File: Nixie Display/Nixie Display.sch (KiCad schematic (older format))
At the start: 34 parts, among them J1 Conn_01x06_Male, J10 Conn_01x02_Male, J12 Conn_01x02_Male, J2 Conn_01x02_Male, J3 Conn_01x20_Male, J4 Conn_01x02_Male, J5 Conn_01x20_Male, J6 Conn_01x02_Male, J7 Conn_01x20_Male, J8 Conn_01x02_Male, U1 WS2812B, U2 WS2812B, U3 WS2812B, U4 WS2812B, U5 WS2812B, U6 WS2812B

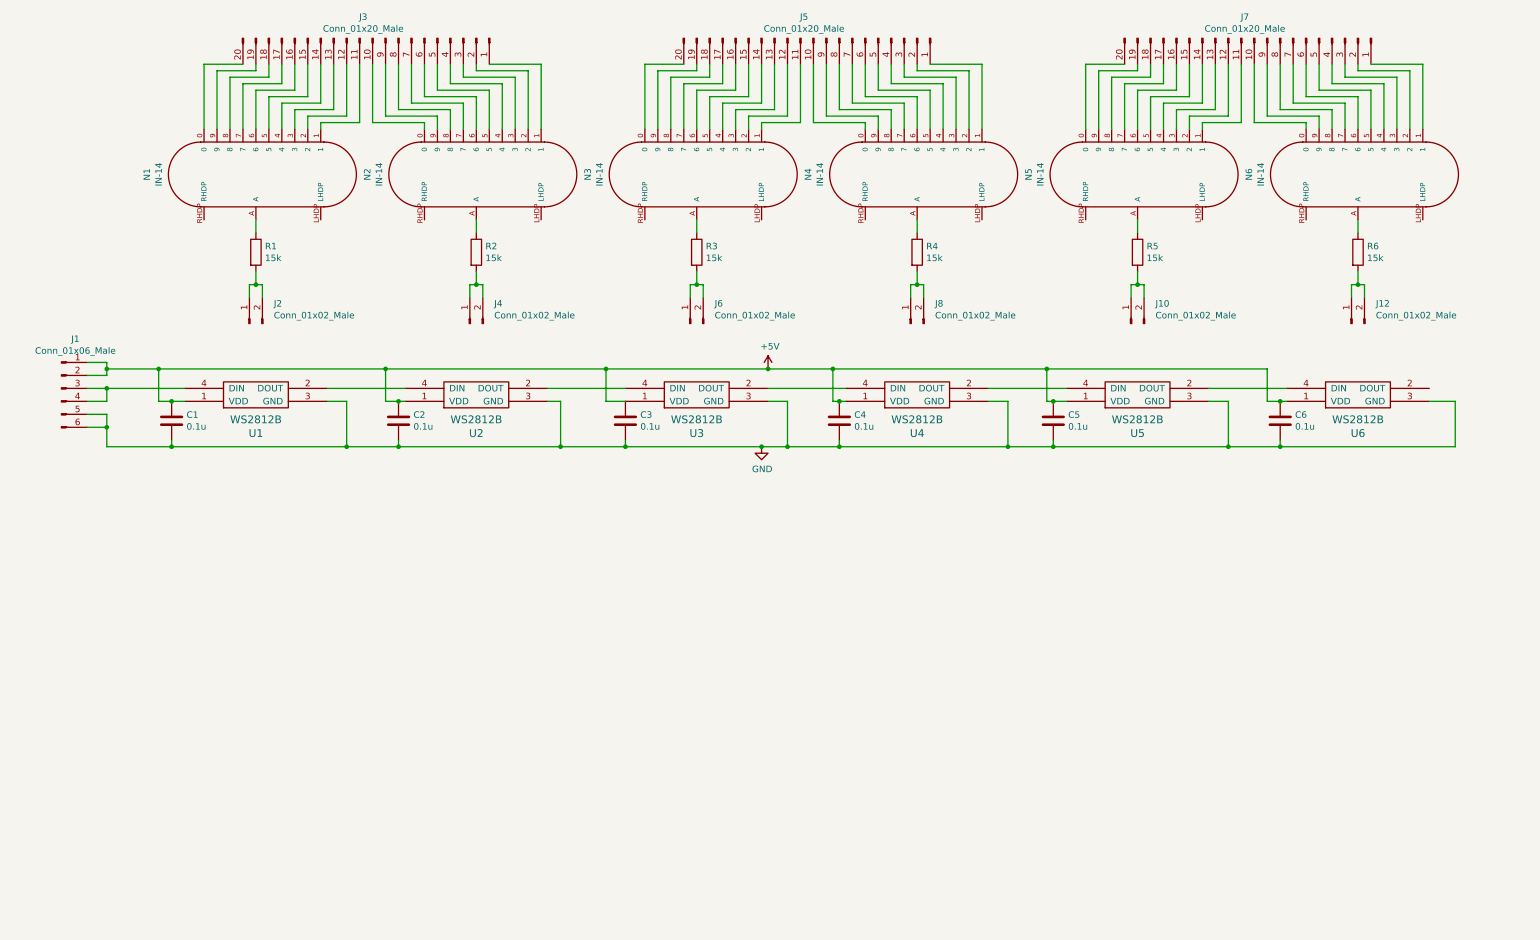
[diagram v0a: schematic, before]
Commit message: Final V1.0 design. Different sized boards for top and bottom layer. Goal for v2.0 is to have matching top and bottom pcbas
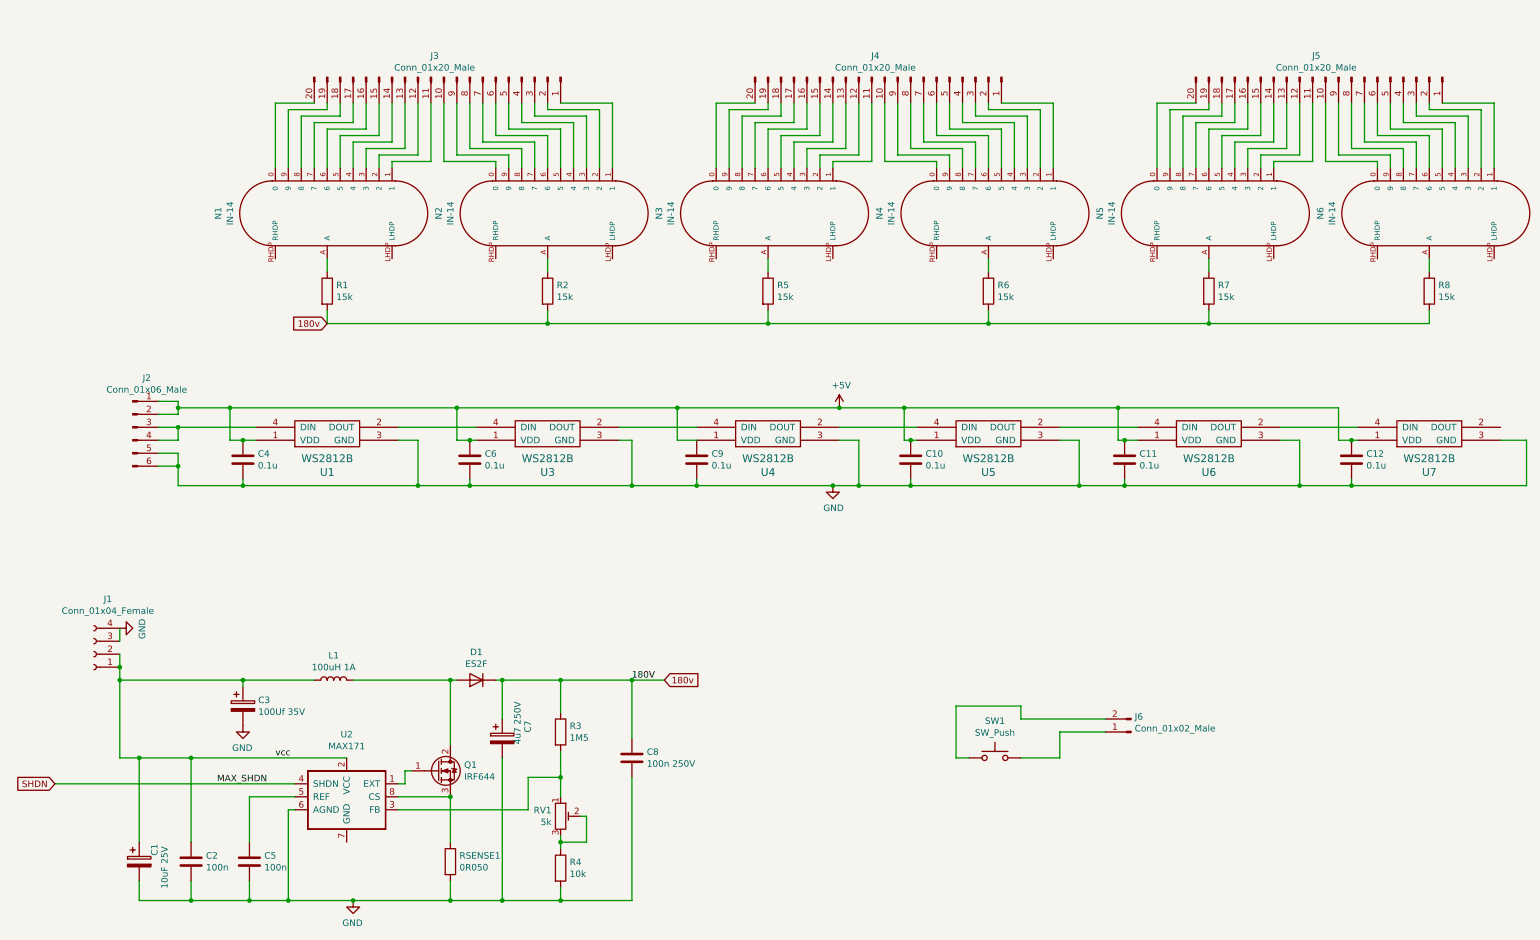
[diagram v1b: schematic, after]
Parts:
- removed C1, C3: 0.1u, Capacitor_SMD:C_0603_1608Metric_Pad1.05x0.95mm_HandSolder, symbol Device:C
- removed J1: Conn_01x06_Male, Connector_PinHeader_2.54mm:PinHeader_1x06_P2.54mm_Vertical, symbol Connector:Conn_01x06_Male
- removed J10, J12, J2, J4, J8: Conn_01x02_Male, Connector_PinHeader_2.54mm:PinHeader_1x02_P2.54mm_Vertical_SMD_Pin1Left, symbol Connector:Conn_01x02_Male
- removed J7: Conn_01x20_Male, Connector_PinHeader_2.54mm:PinHeader_1x20_P2.54mm_Vertical_SMD_Pin1Left, symbol Connector:Conn_01x20_Male
- removed U2: WS2812B, LED_SMD:LED_WS2812B_PLCC4_5.0x5.0mm_P3.2mm, symbol ws2812:WS2812B
- added C1: 10uF 25V, Capacitor_Tantalum_SMD:CP_EIA-7343-31_Kemet-D_Pad2.25x2.55mm_HandSolder, symbol Device:CP
- added C10, C11, C12, C9: 0.1u, Capacitor_SMD:C_0603_1608Metric_Pad1.05x0.95mm_HandSolder, symbol Device:C
- added C3: 100Uf 35V, Capacitor_Tantalum_SMD:CP_EIA-7343-31_Kemet-D_Pad2.25x2.55mm_HandSolder, symbol Device:CP
- added C7: 4u7 250V, Capacitor_SMD:CP_Elec_10x14.3, symbol Device:CP
- added C8: 100n 250V, Capacitor_SMD:C_2220_5650Metric_Pad1.97x5.40mm_HandSolder, symbol Device:C
- added D1: ES2F, Nixie Power and Logic:D_SOD-214AA, symbol Device:D
- added J1: Conn_01x04_Female, Connector_PinHeader_2.54mm:PinHeader_1x04_P2.54mm_Vertical_SMD_Pin1Left, symbol Connector:Conn_01x04_Female
- added J2: Conn_01x06_Male, Connector_PinHeader_2.54mm:PinHeader_1x06_P2.54mm_Vertical, symbol Connector:Conn_01x06_Male
- added J4: Conn_01x20_Male, Connector_PinHeader_2.54mm:PinHeader_1x20_P2.54mm_Vertical_SMD_Pin1Left, symbol Connector:Conn_01x20_Male
- added L1: 100uH 1A, Inductor_SMD:L_Bourns_SDR1806, symbol Device:L
- added Q1: IRF644, Package_TO_SOT_THT:TO-220-3_Vertical, symbol Transistor_FET:BUZ11
- added R7, R8: 15k, Resistor_SMD:R_0603_1608Metric_Pad1.05x0.95mm_HandSolder, symbol Device:R
- added RSENSE1: 0R050, Resistor_SMD:R_2010_5025Metric_Pad1.52x2.65mm_HandSolder, symbol Device:R
- added RV1: 5k, Potentiometer_SMD:Potentiometer_Bourns_3214W_Vertical, symbol Nixie-Display-rescue:R_POT_TRIM-Device_Eric
- added SW1: SW_Push, Button_Switch_SMD:SW_SPST_B3S-1000, symbol Switch:SW_Push
- added U2: MAX171, Nixie Power and Logic:SOIC−8-NARROW, symbol Nixie-Display-rescue:MAX171-Device_Eric
- added U7: WS2812B, LED_SMD:LED_WS2812B_PLCC4_5.0x5.0mm_P3.2mm, symbol ws2812:WS2812B
- C2, C5: value 0.1u -> 100n; footprint Capacitor_SMD:C_0603_1608Metric_Pad1.05x0.95mm_HandSolder -> Capacitor_SMD:C_0805_2012Metric_Pad1.15x1.40mm_HandSolder
- R3: value 15k -> 1M5; footprint Resistor_SMD:R_0603_1608Metric_Pad1.05x0.95mm_HandSolder -> Resistor_SMD:R_2512_6332Metric_Pad1.52x3.35mm_HandSolder
- R4: value 15k -> 10k; footprint Resistor_SMD:R_0603_1608Metric_Pad1.05x0.95mm_HandSolder -> Resistor_SMD:R_0805_2012Metric_Pad1.15x1.40mm_HandSolder
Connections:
- net +5V: now also C10.1, C11.1, C12.1, C9.1, J2.1 (Pin_1), J2.2 (Pin_2), U7.1 (VDD); no longer C2.1, C5.1
- net GND: now also R4.2, C1.2, C10.2, C11.2, C12.2, C3.2, C7.2, C8.2, C9.2, J1.3 (Pin_3), J1.4 (Pin_4), J2.5 (Pin_5), J2.6 (Pin_6), RSENSE1.2, U2.6 (AGND), U7.3 (GND)
- net at N3.0: now also J4.20 (Pin_20); no longer J5.20 (Pin_20)
- net at N3.1: now also J4.11 (Pin_11); no longer J5.11 (Pin_11)
- net at N3.2: now also J4.12 (Pin_12); no longer J5.12 (Pin_12)
- net at N3.3: now also J4.13 (Pin_13); no longer J5.13 (Pin_13)
- net at N3.4: now also J4.14 (Pin_14); no longer J5.14 (Pin_14)
- net at N3.5: now also J4.15 (Pin_15); no longer J5.15 (Pin_15)
- net at N3.6: now also J4.16 (Pin_16); no longer J5.16 (Pin_16)
- net at N3.7: now also J4.17 (Pin_17); no longer J5.17 (Pin_17)
- net at N3.8: now also J4.18 (Pin_18); no longer J5.18 (Pin_18)
- net at N3.9: now also J4.19 (Pin_19); no longer J5.19 (Pin_19)
- net at N3.A: now also R5.1; no longer R3.1
- net at N4.0: now also J4.10 (Pin_10); no longer J5.10 (Pin_10)
- net at N4.1: now also J4.1 (Pin_1); no longer J5.1 (Pin_1)
- net at N4.2: now also J4.2 (Pin_2); no longer J5.2 (Pin_2)
- net at N4.3: now also J4.3 (Pin_3); no longer J5.3 (Pin_3)
- net at N4.4: now also J4.4 (Pin_4); no longer J5.4 (Pin_4)
- net at N4.5: now also J4.5 (Pin_5); no longer J5.5 (Pin_5)
- net at N4.6: now also J4.6 (Pin_6); no longer J5.6 (Pin_6)
- net at N4.7: now also J4.7 (Pin_7); no longer J5.7 (Pin_7)
- net at N4.8: now also J4.8 (Pin_8); no longer J5.8 (Pin_8)
- net at N4.9: now also J4.9 (Pin_9); no longer J5.9 (Pin_9)
- net at N4.A: now also R6.1; no longer R4.1
- net at N5.0: now also J5.20 (Pin_20)
- net at N5.1: now also J5.11 (Pin_11)
- net at N5.2: now also J5.12 (Pin_12)
- net at N5.3: now also J5.13 (Pin_13)
- net at N5.4: now also J5.14 (Pin_14)
- net at N5.5: now also J5.15 (Pin_15)
- net at N5.6: now also J5.16 (Pin_16)
- net at N5.7: now also J5.17 (Pin_17)
- net at N5.8: now also J5.18 (Pin_18)
- net at N5.9: now also J5.19 (Pin_19)
- net at N5.A: now also R7.1; no longer R5.1
- net at N6.0: now also J5.10 (Pin_10)
- net at N6.1: now also J5.1 (Pin_1)
- net at N6.2: now also J5.2 (Pin_2)
- net at N6.3: now also J5.3 (Pin_3)
- net at N6.4: now also J5.4 (Pin_4)
- net at N6.5: now also J5.5 (Pin_5)
- net at N6.6: now also J5.6 (Pin_6)
- net at N6.7: now also J5.7 (Pin_7)
- net at N6.8: now also J5.8 (Pin_8)
- net at N6.9: now also J5.9 (Pin_9)
- net at N6.A: now also R8.1; no longer R6.1
- net 180v: now reaches R1.2
- net 180v: now also R2.2, R3.1, R5.2, R6.2, C7.1, C8.1, D1.1 (K), R7.2, R8.2
- net at U1.2 (DOUT): now also U3.4 (DIN)
- net at U1.4 (DIN): now also J2.3 (Pin_3), J2.4 (Pin_4)
- net at U6.2 (DOUT): now also U7.4 (DIN)
- new net: J6.2 (Pin_2), SW1.1
- new net: J6.1 (Pin_1), SW1.2
- new net: Q1.1 (G), U2.1 (EXT)
- new net: R3.2, RV1.1, U2.3 (FB)
- new net: C5.1, U2.5 (REF)
- new net: Q1.3 (S), RSENSE1.1, U2.8 (CS)
- new net: R4.1, RV1.2, RV1.3
- new net: D1.2 (A), L1.1, Q1.2 (D)
- new net SHDN: U2.4 (SHDN)
- new net vcc: C1.1, C2.1, C3.1, J1.1 (Pin_1), J1.2 (Pin_2), L1.2, U2.2 (VCC)
